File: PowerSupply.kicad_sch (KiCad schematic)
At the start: 8 parts, among them U1 JW5017S

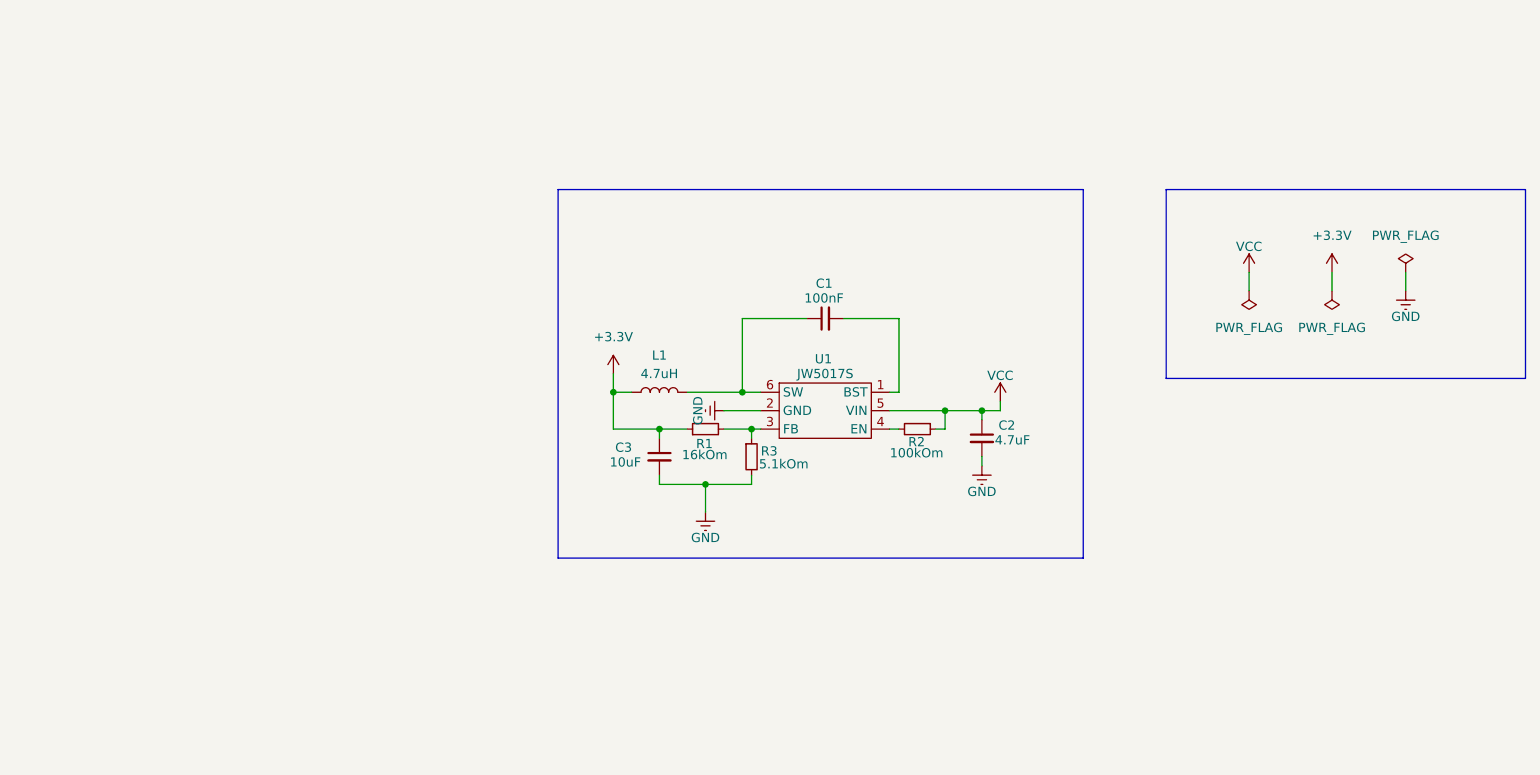
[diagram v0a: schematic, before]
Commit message: Refactor PCB design parameters in endpoint-driver - Adjusted minimum hole-to-hole clearance from 0.25 to 0.24 in the .kicad_pro file for improved spacing.
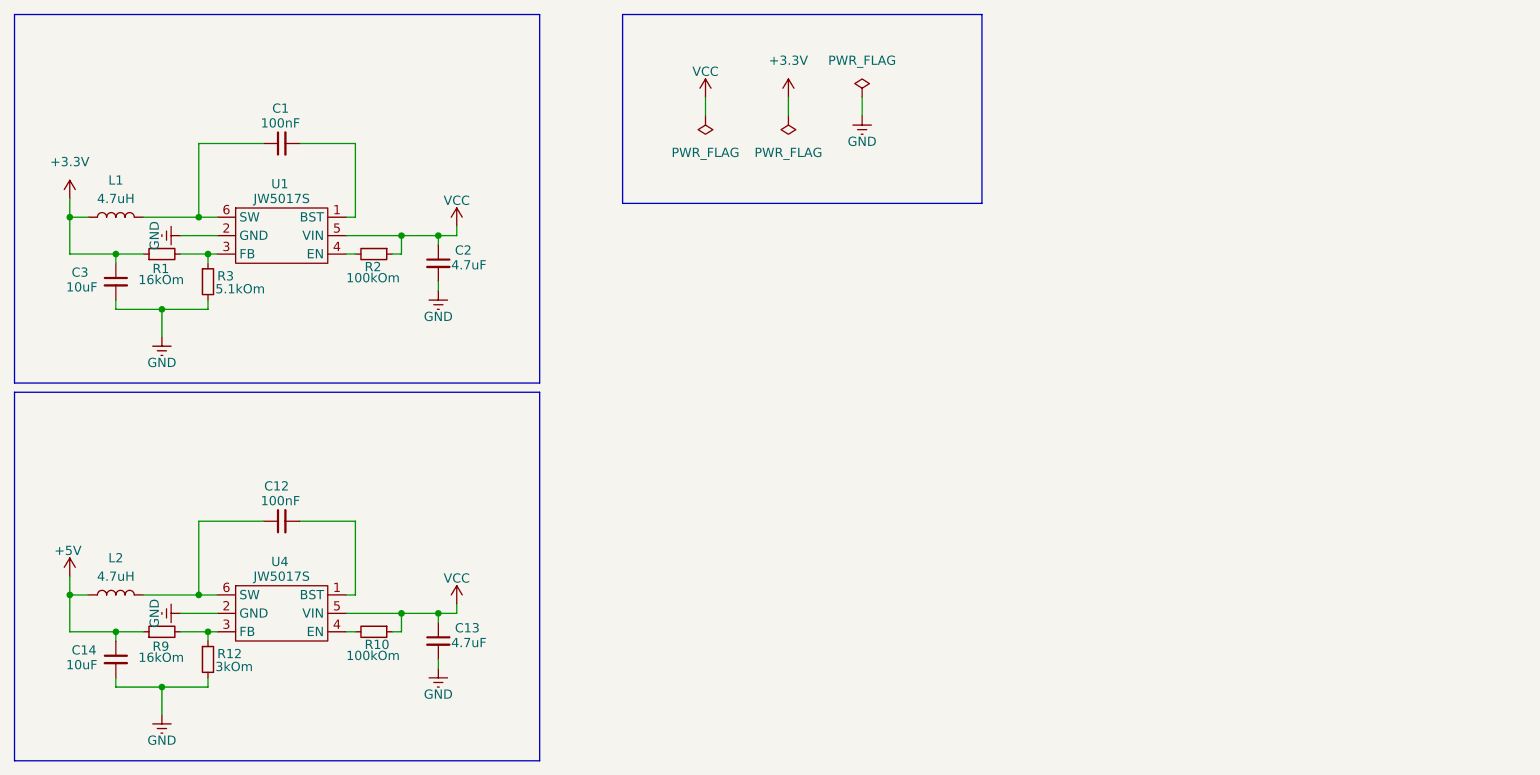
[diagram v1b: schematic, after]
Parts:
- added C12: 100nF, Capacitor_SMD:C_0603_1608Metric, symbol Device:C_Small
- added C13: 4.7uF, Capacitor_SMD:C_0805_2012Metric, symbol Device:C_Small
- added C14: 10uF, Capacitor_SMD:C_0805_2012Metric, symbol Device:C_Small
- added L2: 4.7uH, my_lib:SNR3015K-4R7M, symbol Device:L
- added R10: 100kOm, PCM_Resistor_SMD_AKL:R_0603_1608Metric, symbol Device:R_Small
- added R12: 3kOm, PCM_Resistor_SMD_AKL:R_0603_1608Metric, symbol Device:R_Small
- added R9: 16kOm, PCM_Resistor_SMD_AKL:R_0603_1608Metric, symbol Device:R_Small
- added U4: JW5017S, my_lib:JW5017S, symbol user_library:JW5017S
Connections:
- net GND: now also C13.2, C14.2, R12.2, U4.2 (GND)
- net VCC: now also C13.1, R10.1, U4.5 (VIN)
- new net: R12.1, R9.2, U4.3 (FB)
- new net: R10.2, U4.4 (EN)
- new net: C12.1, L2.2, U4.6 (SW)
- new net: C12.2, U4.1 (BST)
- new net +5V: C14.1, L2.1, R9.1
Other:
- moved on the sheet: C1, C2, C3, L1, R1, R2, R3, U1
